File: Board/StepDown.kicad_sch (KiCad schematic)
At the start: 23 parts, among them U4 TPS548A20RVER

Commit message: Fixing from Review
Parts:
- added C40: 1uF, Capacitor_SMD:C_1210_3225Metric, symbol Device:C
- added C41: 0.1uF, Capacitor_SMD:C_0805_2012Metric, symbol Device:C
- added C42: 2.2nF, Capacitor_SMD:C_0805_2012Metric, symbol Device:C
- R54: value 3 -> 3R
- R55: value 4k7 -> 2R2
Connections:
- net Earth: now also R54.2, C40.1
- net Vin: now also C42.1
- net at C27.2, L1.1, U4.6 (SW)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: now also C41.1
- net at R55.1, U4.19 (VDD): now also C40.2
- net at R36.1, R56.2, U4.2 (PGOOD): now also C42.2
- net at U4.21 (MODE): now also R39.2; no longer R36.2
- net at U4.25 (TRIP): now also R36.2; no longer R39.2
- net at U4.4 (VBST): now also C41.2; no longer R54.2
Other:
- moved on the sheet: C29, R36, R37, R39, R54, R55, R56, R57

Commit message: open findings are fixed, and nothing else changed
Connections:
- net Earth: now also C42.2
- net at R36.1, R56.2, U4.2 (PGOOD): no longer C42.2
- net at U4.21 (MODE): now also R36.2; no longer R39.2
- net at U4.25 (TRIP): now also R39.2; no longer R36.2
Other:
- moved on the sheet: C29, C40, R39, R56, R57

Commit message: V4 review update
- new review from from this version alreaady done
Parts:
- removed C24, C25: 100uF, Capacitor_SMD:C_Elec_6.3x5.4, symbol Device:C_Polarized
- added C24, C25: 47uF, Capacitor_SMD:C_0805_2012Metric, symbol Device:C
- C42: footprint Capacitor_SMD:C_0805_2012Metric -> Capacitor_SMD:C_0402_1005Metric
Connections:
- net Earth: now also C24.2, C25.2
- net Vout: now also C24.1, C25.1
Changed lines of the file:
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@@
+	)
+	(symbol
+		(lib_id "Device:C")
+		(at 189.23 72.39 90)
+		(unit 1)
+		(body_style 1)
+		(exclude_from_sim no)
+		(in_bom yes)
+		(on_board yes)
+		(in_pos_files yes)
+		(dnp no)
+		(property "Reference" "C25"
+			(at 191.008 67.056 90)
+			(show_name no)
+			(do_not_autoplace no)
+			(effects
+				(font
+					(size 1.27 1.27)
+				)
+				(justify left)
+			)
+		)
+		(property "Value" "47uF"
+			(at 192.024 69.088 90)
+			(show_name no)
+			(do_not_autoplace no)
+			(effects
+				(font
+					(size 1.27 1.27)
+				)
+				(justify left)
+			)
+		)
+		(property "Footprint" "Capacitor_SMD:C_0805_2012Metric"
+			(at 193.04 71.4248 0)
+			(hide yes)
+			(show_name no)
+			(do_not_autoplace no)
+			(effects
+				(font
+					(size 1.27 1.27)
+				)
+			)
+		)
+		(property "Datasheet" ""
+			(at 189.23 72.39 0)
+			(hide yes)
+			(show_name no)
+			(do_not_autoplace no)
+			(effects
+				(font
+					(size 1.27 1.27)
+				)
+			)
+		)
+		(property "Description" "Unpolarized capacitor"
+			(at 189.23 72.39 0)
+			(hide yes)
+			(show_name no)
+			(do_not_autoplace no)
+			(effects
+				(font
+					(size 1.27 1.27)
+				)
+			)
+		)
+		(pin "2"
+		)
+		(pin "1"
+		)
+		(instances
+			(project "SlimeVR_Dock"
+				(path "/06ff9557-1f9b-4670-8a34-bb7684a016dd/9328ec89-1532-462d-95ef-1baa495e4b70"
+					(reference "C25")
+					(unit 1)
+				)
+			)
+		)
 	)
 	(symbol
@@
 	)
 	(symbol
-		(lib_id "Device:C_Polarized")
-		(at 189.23 72.39 90)
-		(unit 1)
-		(body_style 1)
-		(exclude_from_sim no)
-		(in_bom yes)
-		(on_board yes)
-		(in_pos_files yes)
-		(dnp no)
-		(property "Reference" "C24"
-			(at 188.976 67.31 90)
-			(show_name no)
-			(do_not_autoplace no)
-			(effects
-				(font
-					(size 1.27 1.27)
-				)
-			)
-		)
-		(property "Value" "100uF"
-			(at 189.23 69.088 90)
-			(show_name no)
-			(do_not_autoplace no)
-			(effects
-				(font
-					(size 1.27 1.27)
-				)
-			)
-		)
-		(property "Footprint" "Capacitor_SMD:C_Elec_6.3x5.4"
-			(at 193.04 71.4248 0)
-			(hide yes)
-			(show_name no)
-			(do_not_autoplace no)
-			(effects
-				(font
-					(size 1.27 1.27)
-				)
-			)
-		)
-		(property "Datasheet" ""
-			(at 189.23 72.39 0)
-			(hide yes)
-			(show_name no)
-			(do_not_autoplace no)
-			(effects
-				(font
-					(size 1.27 1.27)
-				)
-			)
-		)
-		(property "Description" "Polarized capacitor"
-			(at 189.23 72.39 0)
-			(hide yes)
-			(show_name no)
-			(do_not_autoplace no)
-			(effects
-				(font
-					(size 1.27 1.27)
-				)
-			)
-		)
-		(pin "1"
-		)
-		(pin "2"
-		)
-		(instances
-			(project "SlimeVR_Dock"
-				(path "/06ff9557-1f9b-4670-8a34-bb7684a016dd/9328ec89-1532-462d-95ef-1baa495e4b70"
-					(reference "C24")
-					(unit 1)
-				)
-			)
-		)
-	)
-	(symbol
 		(lib_id "Device:R")
 		(at 109.22 119.38 90)
@@
 	)
 	(symbol
-		(lib_id "Device:C_Polarized")
-		(at 189.23 81.28 90)
-		(unit 1)
-		(body_style 1)
-		(exclude_from_sim no)
-		(in_bom yes)
-		(on_board yes)
-		(in_pos_files yes)
-		(dnp no)
-		(property "Reference" "C25"
-			(at 189.23 76.2 90)
-			(show_name no)
-			(do_not_autoplace no)
-			(effects
-				(font
-					(size 1.27 1.27)
-				)
-			)
-		)
-		(property "Value" "100uF"
-			(at 189.23 77.978 90)
-			(show_name no)
-			(do_not_autoplace no)
-			(effects
-				(font
-					(size 1.27 1.27)
-				)
-			)
-		)
-		(property "Footprint" "Capacitor_SMD:C_Elec_6.3x5.4"
-			(at 193.04 80.3148 0)
-			(hide yes)
-			(show_name no)
-			(do_not_autoplace no)
-			(effects
-				(font
-					(size 1.27 1.27)
-				)
-			)
-		)
-		(property "Datasheet" ""
-			(at 189.23 81.28 0)
-			(hide yes)
-			(show_name no)
-			(do_not_autoplace no)
-			(effects
-				(font
-					(size 1.27 1.27)
-				)
-			)
-		)
-		(property "Description" "Polarized capacitor"
-			(at 189.23 81.28 0)
-			(hide yes)
-			(show_name no)
-			(do_not_autoplace no)
-			(effects
-				(font
-					(size 1.27 1.27)
-				)
-			)
-		)
-		(pin "1"
-		)
-		(pin "2"
-		)
-		(instances
-			(project "SlimeVR_Dock"
-				(path "/06ff9557-1f9b-4670-8a34-bb7684a016dd/9328ec89-1532-462d-95ef-1baa495e4b70"
-					(reference "C25")
-					(unit 1)
-				)
-			)
-		)
-	)
-	(symbol
 		(lib_id "Device:R")
 		(at 176.53 105.41 270)
@@
 	(symbol
 		(lib_id "Device:C")
+		(at 189.23 81.28 90)
+		(unit 1)
+		(body_style 1)
+		(exclude_from_sim no)
+		(in_bom yes)
+		(on_board yes)
+		(in_pos_files yes)
+		(dnp no)
+		(property "Reference" "C24"
+			(at 191.008 75.946 90)
+			(show_name no)
+			(do_not_autoplace no)
+			(effects
+				(font
+					(size 1.27 1.27)
+				)
+				(justify left)
+			)
+		)
+		(property "Value" "47uF"
+			(at 192.024 77.978 90)
+			(show_name no)
+			(do_not_autoplace no)
+			(effects
+				(font
+					(size 1.27 1.27)
+				)
+				(justify left)
+			)
+		)
+		(property "Footprint" "Capacitor_SMD:C_0805_2012Metric"
+			(at 193.04 80.3148 0)
+			(hide yes)
+			(show_name no)
+			(do_not_autoplace no)
+			(effects
+				(font
+					(size 1.27 1.27)
+				)
+			)
+		)
+		(property "Datasheet" ""
+			(at 189.23 81.28 0)
+			(hide yes)
+			(show_name no)
+			(do_not_autoplace no)
+			(effects
+				(font
+					(size 1.27 1.27)
+				)
+			)
+		)
+		(property "Description" "Unpolarized capacitor"
+			(at 189.23 81.28 0)
+			(hide yes)
+			(show_name no)
+			(do_not_autoplace no)
+			(effects
+				(font
+					(size 1.27 1.27)
+				)
+			)
+		)
+		(pin "2"
+		)
+		(pin "1"
+		)
+		(instances
+			(project "SlimeVR_Dock"
+				(path "/06ff9557-1f9b-4670-8a34-bb7684a016dd/9328ec89-1532-462d-95ef-1baa495e4b70"
+					(reference "C24")
+					(unit 1)
+				)
+			)
+		)
+	)
+	(symbol
+		(lib_id "Device:C")
 		(at 101.6 90.17 270)
 		(unit 1)
@@
 			)
 		)
-		(property "Footprint" "Capacitor_SMD:C_0805_2012Metric"
+		(property "Footprint" "Capacitor_SMD:C_0402_1005Metric"
 			(at 97.79 91.1352 0)
 			(hide yes)

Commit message: Updated Inductor for Isat > 17A
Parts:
- L1: footprint Inductor_SMD:L_Vishay_IHLP-2525 -> Inductor_SMD:L_Coilcraft_XAL7030-222
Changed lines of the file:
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@@
 			)
 		)
-		(property "Footprint" "Inductor_SMD:L_Vishay_IHLP-2525"
+		(property "Footprint" "Inductor_SMD:L_Coilcraft_XAL7030-222"
 			(at 179.07 93.98 0)
 			(hide yes)

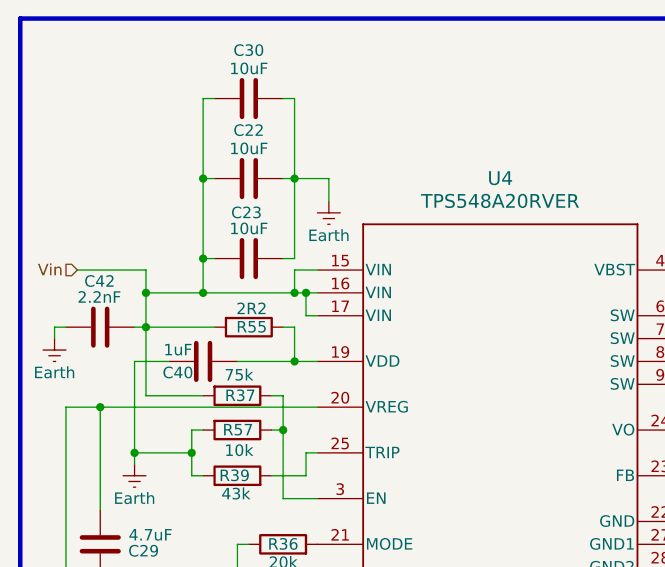
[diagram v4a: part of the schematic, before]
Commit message: Board and schema update
curent mesuring resistors swap for bigger
some more grounding was done
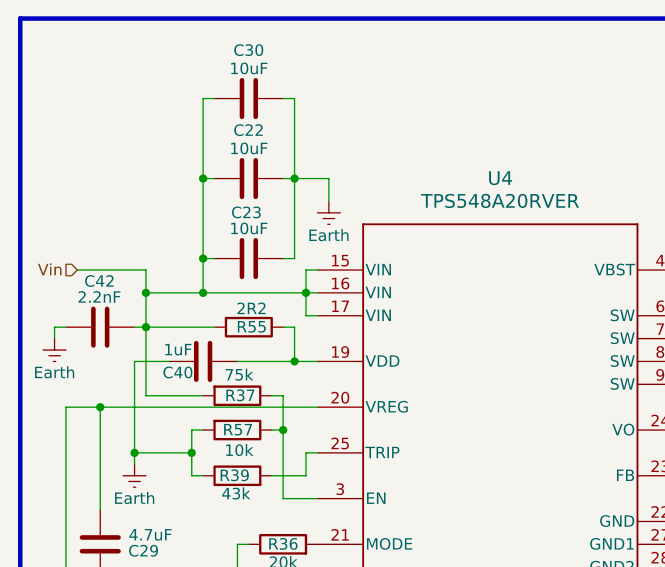
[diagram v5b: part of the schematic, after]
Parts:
- L1: footprint Inductor_SMD:L_Coilcraft_XAL7030-222 -> Inductor_SMD:L_Coilcraft_XAL7070-XXX
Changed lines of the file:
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@@
-	)
-	(junction
-		(at 123.19 86.36)
-		(diameter 0)
-		(color 0 0 0 0)
 	)
 	(junction
@@
 	(wire
 		(pts
-			(xy 124.46 86.36) (xy 123.19 86.36)
-		)
-		(stroke
-			(width 0)
-			(type default)
-		)
-	)
-	(wire
-		(pts
 			(xy 124.46 106.68) (xy 124.46 104.14)
 		)
@@
 	(wire
 		(pts
-			(xy 123.19 86.36) (xy 123.19 83.82)
+			(xy 124.46 86.36) (xy 124.46 83.82)
 		)
 		(stroke
@@
 	(wire
 		(pts
-			(xy 113.03 86.36) (xy 123.19 86.36)
+			(xy 113.03 86.36) (xy 124.46 86.36)
 		)
 		(stroke
@@
 	(wire
 		(pts
-			(xy 123.19 83.82) (xy 125.73 83.82)
+			(xy 124.46 83.82) (xy 125.73 83.82)
 		)
 		(stroke
@@
 			)
 		)
-		(property "Footprint" "Inductor_SMD:L_Coilcraft_XAL7030-222"
+		(property "Footprint" "Inductor_SMD:L_Coilcraft_XAL7070-XXX"
 			(at 179.07 93.98 0)
 			(hide yes)

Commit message: New review completed version
-Board ONLY changes no documentation updated YET
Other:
- company: (none) -> Skaut0071
- title: (none) -> 20V to 5V 8,5A Stepdown
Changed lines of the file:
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@@
 	(generator_version "10.0")
 	(paper "A4")
+	(title_block
+		(title "20V to 5V 8,5A Stepdown")
+		(date "2026-09-21")
+		(rev "2.1")
+		(company "Skaut0071")
+	)
 	(rectangle
 		(start 92.71 55.88)
